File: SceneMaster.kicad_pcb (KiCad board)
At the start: 4 copper layers, 50 x 30 mm, 102 parts, among them J1 TYPE-C-31-M-12, J11 PowerIn, J12 PowerOut, J13 LED3, J14 LED4, J15 LED5, J2 SPK_R, J3 LED1, J4 LED2, J5 LED6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

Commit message: Change sensor & speaker connectors to 1mm SH
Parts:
- J11, J12, J13, J14, J15, J3, J4, J5: footprint Connector_JST:JST_SUR_SM02B-SURS-TF_1x02-1MP_P0.80mm_Horizontal -> ant:JST_SUR_SM02B-SURS-TF_1x02-1MP_P0.80mm_Horizontal
- J2, J9: footprint Connector_JST:JST_SUR_SM02B-SURS-TF_1x02-1MP_P0.80mm_Horizontal -> ant:JST_SH_SM02B-SRSS-TB_1x02-1MP_P1.00mm_Horizontal
- J6, J7, J8: footprint Connector_JST:JST_SUR_SM03B-SURS-TF_1x03-1MP_P0.80mm_Horizontal -> ant:JST_SH_SM03B-SRSS-TB_1x03-1MP_P1.00mm_Horizontal
- moved D3 28.3 mm to (113.0, 80.0)
- moved R13 24.9 mm to (113.0, 78.8)
- moved R16 11.1 mm to (140.0, 72.8), turned to 90 degrees
- moved TP5 5.41 mm to (148.0, 66.2)
- moved TP10 5.32 mm to (139.0, 67.2)
- moved TP1 4.28 mm to (131.0, 69.2)
- moved R17 4.27 mm to (141.0, 72.8), turned to 90 degrees
- moved TP2 4.27 mm to (139.0, 69.2)
- moved D2 3.82 mm to (137.0, 72.8), turned to 180 degrees
- moved TP14 3.35 mm to (122.5, 69.2)
- moved TP15 3.35 mm to (110.0, 69.2)
- moved TP21 3.35 mm to (114.5, 69.2)
- moved TP22 3.35 mm to (102.0, 69.2)
- moved R12 3.20 mm to (139.0, 72.8), turned to 90 degrees
- moved C22 1.27 mm to (101.5, 73.0), turned to 90 degrees
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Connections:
- J6 pad 2: Net-(J6-Pad2) -> GND
- J6 pad 3: GND -> Net-(J6-Pad3)
- J7 pad 2: Net-(J7-Pad2) -> GND
- J7 pad 3: GND -> Net-(J7-Pad3)
- J8 pad 2: Net-(J8-Pad2) -> GND
- J8 pad 3: GND -> Net-(R17-Pad2)
- R16 pad 2: Net-(J7-Pad2) -> Net-(J7-Pad3)
- R17 pad 2: Net-(J8-Pad2) -> Net-(R17-Pad2)
- R18 pad 2: Net-(J6-Pad2) -> Net-(J6-Pad3)
- TP1 pad 1: Net-(J7-Pad2) -> Net-(J7-Pad3)
- TP10 pad 1: Net-(J6-Pad2) -> Net-(J6-Pad3)
- TP2 pad 1: Net-(J8-Pad2) -> Net-(R17-Pad2)
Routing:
- net Net-(J7-Pad3): track 0.00 -> 18.2 mm
- net /SPI_CS: track 29.9 -> 17.8 mm, vias 2 -> 0
- net Net-(R17-Pad2): track 0.00 -> 12.0 mm
- net /SENS1: track 13.9 -> 2.99 mm
- net Net-(J6-Pad3): track 0.00 -> 6.95 mm
- net /UART_TX: track 6.95 -> 12.7 mm
- net GND: track 72.7 -> 77.3 mm, vias 35 -> 33
- net /SENS2: track 7.36 -> 2.78 mm
- net Net-(J7-Pad2): track 4.29 -> 0.00 mm
- net Net-(J6-Pad2): track 4.06 -> 0.00 mm
- net Net-(J8-Pad2): track 4.05 -> 0.00 mm
- net +3V3: track 33.0 -> 35.8 mm, vias 11 -> 10
- net +5V: track 25.2 -> 23.2 mm
- net /SWDIO: track 17.8 -> 19.5 mm
- net /SPK_R-: track 12.0 -> 13.6 mm
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
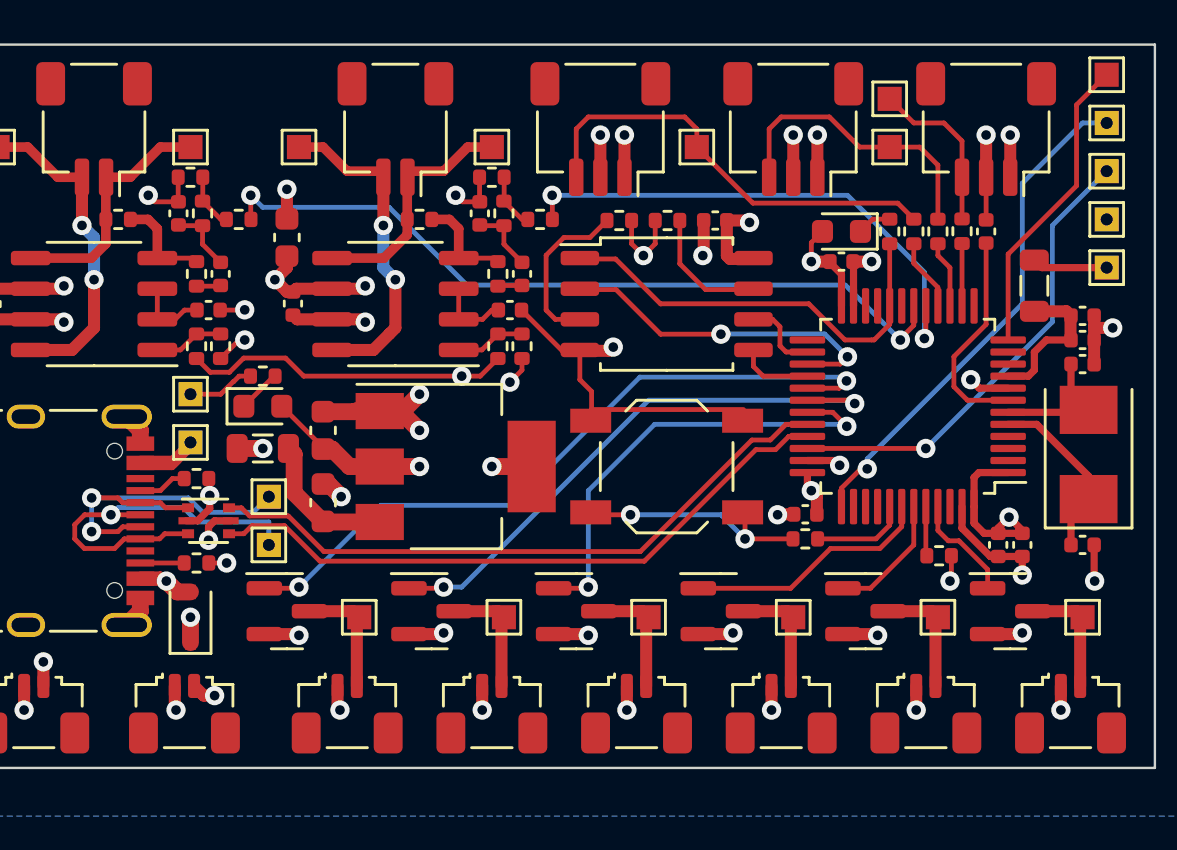
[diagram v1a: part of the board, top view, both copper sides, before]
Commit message: Resize some vias to 0.7/0.3
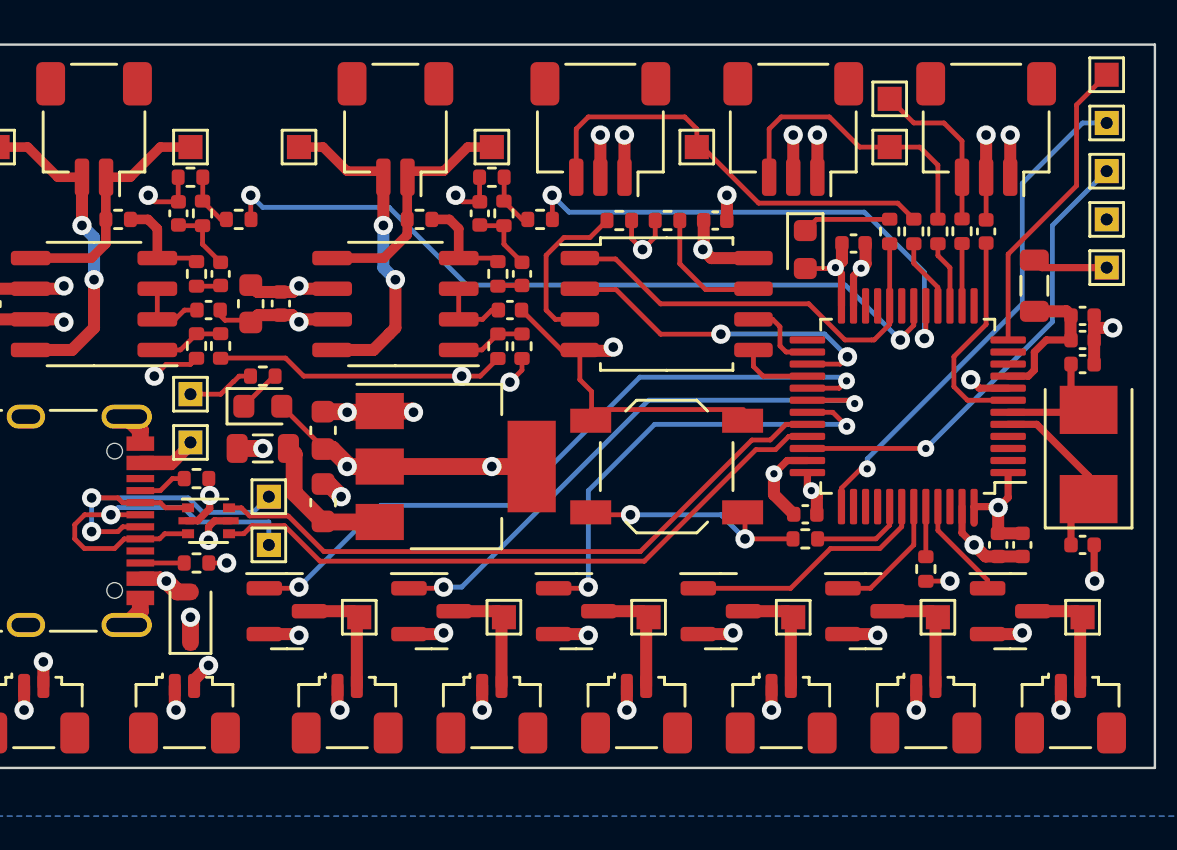
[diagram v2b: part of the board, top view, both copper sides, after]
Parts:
- moved C21 3.13 mm to (112.5, 75.8), turned to -90 degrees
- moved D2 1.68 mm to (135.5, 73.5), turned to -90 degrees
- moved R22 1.00 mm to (111.2, 77.5)
- moved R23 1.00 mm to (110.2, 77.5)
- moved C4 0.90 mm to (137.5, 73.2)
- moved R14 0.78 mm to (140.5, 86.8), turned to -90 degrees
- moved C17 0.50 mm to (113.8, 75.7)
- turned C13 to 0 degrees
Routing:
- net GND: track 77.3 -> 74.6 mm, vias 33 -> 30
- net Net-(D2-Pad1): track 1.42 -> 3.70 mm
- net /MUTE: track 13.6 -> 12.1 mm
- net +5V: track 23.2 -> 22.3 mm, vias 16 -> 15

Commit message: First SGGS re-route
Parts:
- TP14: value SPK_R+ -> SPK_R-
- TP15: value SKP_L+ -> SKP_L-
- TP21: value SPK_R- -> SPK_R+
- TP22: value SKP_L- -> SKP_L+
- TP6, TP7: footprint TestPoint:TestPoint_THTPad_1.0x1.0mm_Drill0.5mm -> TestPoint:TestPoint_Pad_1.0x1.0mm
- moved TP21 8.31 mm to (122.5, 67.0)
- moved TP22 8.31 mm to (110.0, 67.0)
- moved R21 1.03 mm to (120.5, 72.5)
- moved R25 1.03 mm to (108.0, 72.5)
- moved TP19 0.75 mm to (148.0, 75.0)
- moved TP20 0.75 mm to (148.0, 73.0)
- moved TP3 0.75 mm to (148.0, 69.0)
- moved TP4 0.75 mm to (148.0, 71.0)
- moved TP5 0.75 mm to (148.0, 67.0)
- moved C19 0.50 mm to (101.2, 75.8)
- moved C22 0.25 mm to (101.2, 73.0)
- moved R13 0.25 mm to (113.0, 78.5)
- moved TP1 0.25 mm to (131.0, 69.0)
- moved TP10 0.25 mm to (139.0, 67.0)
- moved TP14 0.25 mm to (122.5, 69.0)
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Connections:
- J2 pad 1: /SPK_R+ -> /SPK_R-
- J2 pad 2: /SPK_R- -> /SPK_R+
- J9 pad 1: /SPK_L+ -> /SPK_L-
- J9 pad 2: /SPK_L- -> /SPK_L+
- TP14 pad 1: /SPK_R+ -> /SPK_R-
- TP15 pad 1: /SPK_L+ -> /SPK_L-
- TP21 pad 1: /SPK_R- -> /SPK_R+
- TP22 pad 1: /SPK_L- -> /SPK_L+
- TP6 pad 1: /D- -> /USB_DN
- TP7 pad 1: /D+ -> /USB_DP
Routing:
- net +5V: track 22.3 -> 117.3 mm, vias 15 -> 13
- net +3V3: track 36.1 -> 118.6 mm, vias 10 -> 9
- net /D+: track 16.5 -> 8.35 mm, vias 1 -> 0
- net /D-: track 15.5 -> 7.42 mm
- net /SPK_L+: track 10.1 -> 14.4 mm, vias 0 -> 2
- net /SPK_R+: track 10.1 -> 14.3 mm, vias 0 -> 2
- net /PWM_AUDIO_R: track 21.9 -> 18.9 mm
- net GND: track 74.6 -> 71.8 mm, vias 30 -> 36
- net Net-(R24-Pad1): track 4.18 -> 2.88 mm
- net Net-(R20-Pad1): track 4.18 -> 2.88 mm
- net /OSC_OUT: track 5.58 -> 4.41 mm
- net Net-(R3-Pad1): track 9.99 -> 11.1 mm
- net /VBUS: track 17.2 -> 16.1 mm
- net /USB_DP: track 26.9 -> 28.0 mm
- net /OSC_IN: track 7.38 -> 6.35 mm
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- added copper zone on In2.Cu, net GND
- removed copper zone on In2.Cu, net +3V3
- removed copper zone on In2.Cu, net +5V

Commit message: Last changes before prototype run
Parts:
- removed TP19: 3v3, TestPoint:TestPoint_THTPad_1.0x1.0mm_Drill0.5mm
- removed TP20: GND, TestPoint:TestPoint_THTPad_1.0x1.0mm_Drill0.5mm
- removed TP3: SWCLK, TestPoint:TestPoint_THTPad_1.0x1.0mm_Drill0.5mm
- removed TP4: SWDIO, TestPoint:TestPoint_THTPad_1.0x1.0mm_Drill0.5mm
- removed TP5: UART_TX, TestPoint:TestPoint_Pad_1.0x1.0mm
- added J10: Conn_01x08_Male, ant:SOIC_clipProgSmall, F.Cu at (149.3, 70.6)
- added REF**: MountingHole_2.1mm, MountingHole:MountingHole_2.1mm, F.Cu at (101.4, 90.3)
- added REF**: MountingHole_2.1mm, MountingHole:MountingHole_2.1mm, F.Cu at (148.6, 66.4)
- FB1, FB2: value 600Ω@100MHz -> 100Ω@100MHz
- J2, J9: footprint ant:JST_SH_SM02B-SRSS-TB_1x02-1MP_P1.00mm_Horizontal -> Connector_Hirose:Hirose_DF13C_CL535-0402-2-51_1x02-1MP_P1.25mm_Vertical
- Y1: footprint Crystal:Crystal_SMD_5032-2Pin_5.0x3.2mm -> Crystal:Crystal_SMD_TXC_7A-2Pin_5x3.2mm
- moved J2 1.30 mm to (117.2, 68.5)
- moved J9 1.30 mm to (104.7, 68.5)
- moved Y1 0.35 mm to (146.9, 82.0)
- moved FB1 0.32 mm to (145.1, 74.7), turned to 0 degrees
- moved R6 0.15 mm to (112.0, 72.4)
- moved R21 0.10 mm to (120.5, 72.4)
- moved R25 0.10 mm to (108.0, 72.4)
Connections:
- U4 pad 19: unconnected-(U4-Pad19) -> /MUTE
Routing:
- net /MUTE: track 12.3 -> 36.0 mm, vias 1 -> 2
- net +3V3: track 118.6 -> 103.6 mm, vias 9 -> 10
- net +5V: track 117.3 -> 130.3 mm, vias 13 -> 14
- net /SPK_L+: track 14.4 -> 18.3 mm
- net /SPK_R+: track 14.3 -> 17.8 mm
- net /SWDIO: track 18.9 -> 21.4 mm, vias 1 -> 2
- net /UART_TX: track 12.4 -> 14.7 mm, vias 0 -> 1
- net GND: track 71.8 -> 73.4 mm, vias 36 -> 43
- net /PWM_AUDIO_L: track 31.2 -> 32.4 mm
- net /SWCLK: track 20.8 -> 21.7 mm, vias 1 -> 2
- net /OSC_OUT: track 4.41 -> 5.09 mm
- net /OSC_IN: track 6.35 -> 7.00 mm
- net /PWM_AUDIO_R: track 18.9 -> 18.3 mm
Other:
- outline, holes or cut-outs redrawn
- board text added: "JLCJLCJLCJLC"
- board text added: "Modelectronics"
- board text added: "SceneMaster"
- board text added: "v1.0"

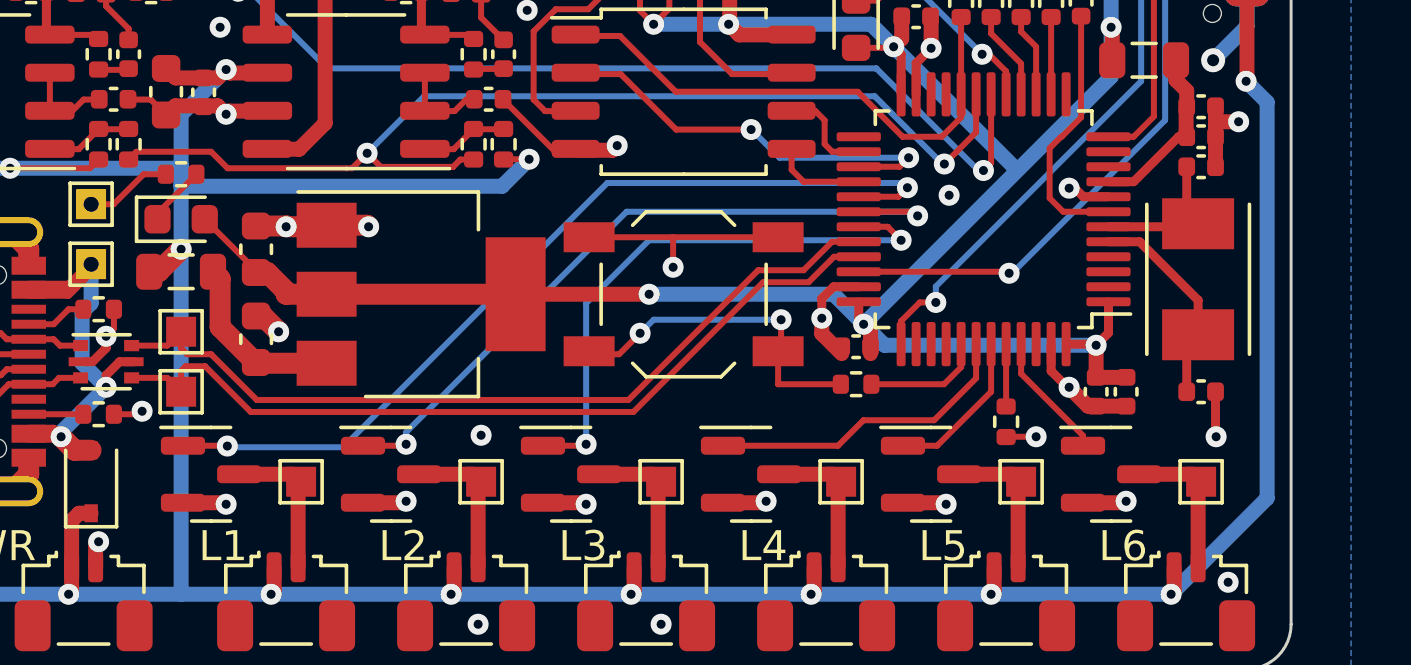
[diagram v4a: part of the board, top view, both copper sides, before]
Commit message: Add gate resistor to mosfets
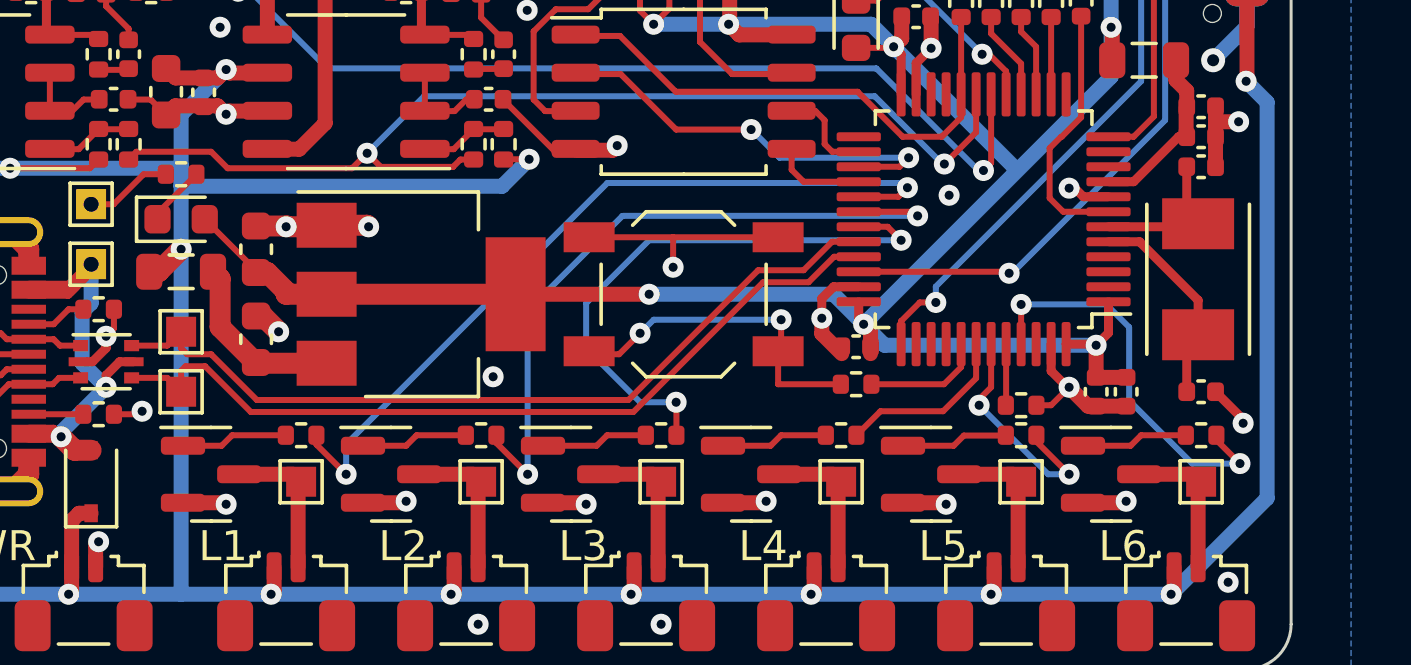
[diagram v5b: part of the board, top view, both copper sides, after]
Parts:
- added R26: 1k, Resistor_SMD:R_0402_1005Metric, F.Cu at (117.0, 87.2)
- added R27: 1k, Resistor_SMD:R_0402_1005Metric, F.Cu at (123.0, 87.2)
- added R28: 1k, Resistor_SMD:R_0402_1005Metric, F.Cu at (147.0, 87.2)
- added R29: 1k, Resistor_SMD:R_0402_1005Metric, F.Cu at (129.0, 87.2)
- added R30: 1k, Resistor_SMD:R_0402_1005Metric, F.Cu at (135.0, 87.2)
- added R31: 1k, Resistor_SMD:R_0402_1005Metric, F.Cu at (141.0, 87.2)
- moved R14 0.74 mm to (141.0, 86.2), turned to 0 degrees
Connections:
- Q1 pad 1: /LED1 -> Net-(Q1-Pad1)
- Q2 pad 1: /LED2 -> Net-(Q2-Pad1)
- Q3 pad 1: /LED6 -> Net-(Q3-Pad1)
- Q4 pad 1: /LED3 -> Net-(Q4-Pad1)
- Q5 pad 1: /LED4 -> Net-(Q5-Pad1)
- Q6 pad 1: /LED5 -> Net-(Q6-Pad1)
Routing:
- net /LED6: track 4.24 -> 13.5 mm, vias 0 -> 2
- net /LED4: track 10.5 -> 5.91 mm
- net Net-(Q6-Pad1): track 0.00 -> 3.58 mm
- net Net-(Q5-Pad1): track 0.00 -> 3.57 mm
- net Net-(Q3-Pad1): track 0.00 -> 3.57 mm
- net Net-(Q4-Pad1): track 0.00 -> 3.57 mm
- net Net-(Q2-Pad1): track 0.00 -> 3.57 mm
- net Net-(Q1-Pad1): track 0.00 -> 3.57 mm
- net /LED5: track 5.27 -> 7.91 mm, vias 0 -> 2
- net /LED1: track 29.1 -> 26.8 mm
- net /LED3: track 18.6 -> 19.3 mm
- net GND: track 73.4 -> 73.7 mm, vias 43 -> 42

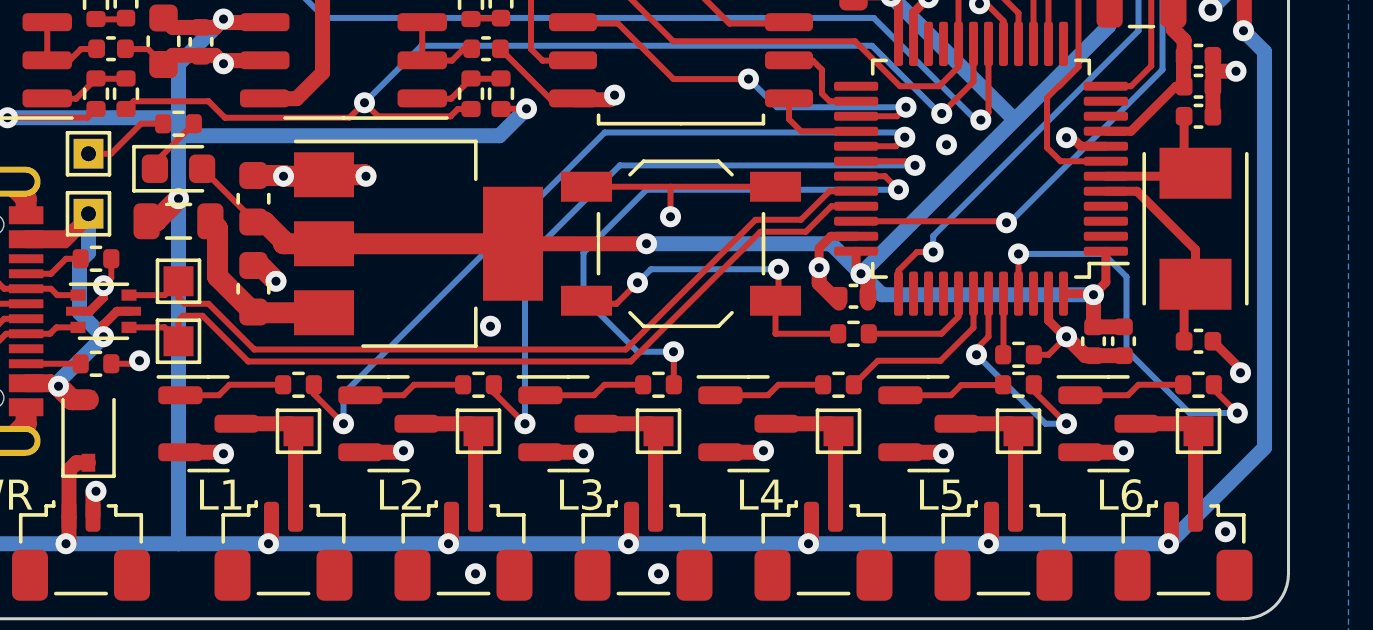
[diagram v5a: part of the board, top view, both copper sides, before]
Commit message: Add USB enable pull up
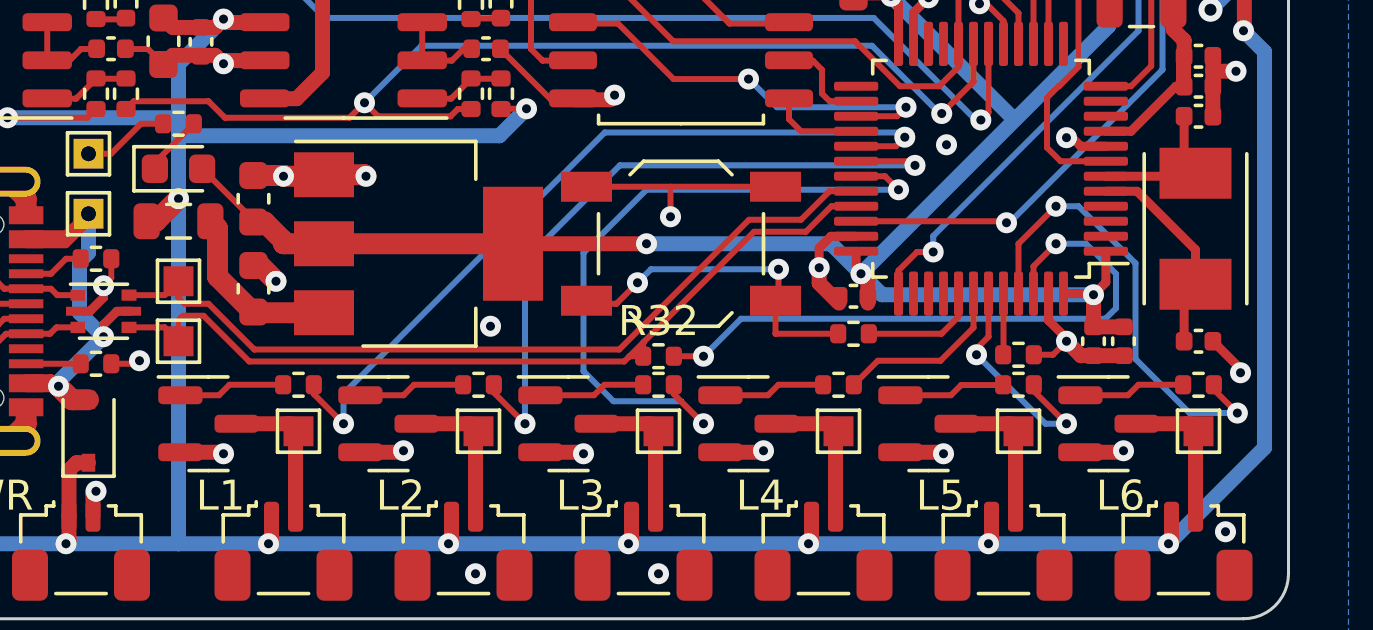
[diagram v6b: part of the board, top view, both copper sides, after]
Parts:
- added R32: 1k, Resistor_SMD:R_0402_1005Metric, F.Cu at (129.0, 86.2)
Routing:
- net /USB_EN: track 0.00 -> 20.9 mm, vias 0 -> 2
- net /LED3: track 19.3 -> 23.4 mm
- net /LED6: track 13.5 -> 15.5 mm
- net /USB_DP: track 28.0 -> 28.9 mm
